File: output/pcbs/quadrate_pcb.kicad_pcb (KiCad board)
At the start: 2 copper layers, 99.2 x 99.2 mm, 19 parts

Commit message: ortho
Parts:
- added S18: , MX, F.Cu at (233.2, 195.2)
- moved S16 31.5 mm to (195.2, 195.2), turned to 0 degrees
- moved S17 24.5 mm to (214.2, 195.2), turned to 0 degrees
- moved S7 13.3 mm to (190.4, 152.4)
- moved S8 13.3 mm to (190.4, 133.3)
- moved S9 13.3 mm to (190.4, 114.3)
- moved S10 11.4 mm to (209.4, 152.4)
- moved S11 11.4 mm to (209.4, 133.3)
- moved S12 11.4 mm to (209.4, 114.3)
- moved S4 9.53 mm to (171.4, 152.4)
- moved S5 9.52 mm to (171.4, 133.3)
- moved S6 9.52 mm to (171.4, 114.3)
- moved S13 7.62 mm to (228.4, 152.4)
- moved TRRS1 7.62 mm to (241.7, 169.5)
- moved S14 7.62 mm to (228.4, 133.3)
- moved S15 7.62 mm to (228.4, 114.3)
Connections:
- net thumbfan_far_home renamed thumbfan_home_home
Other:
- board size 99.2 x 99.2 mm -> 100 x 100 mm

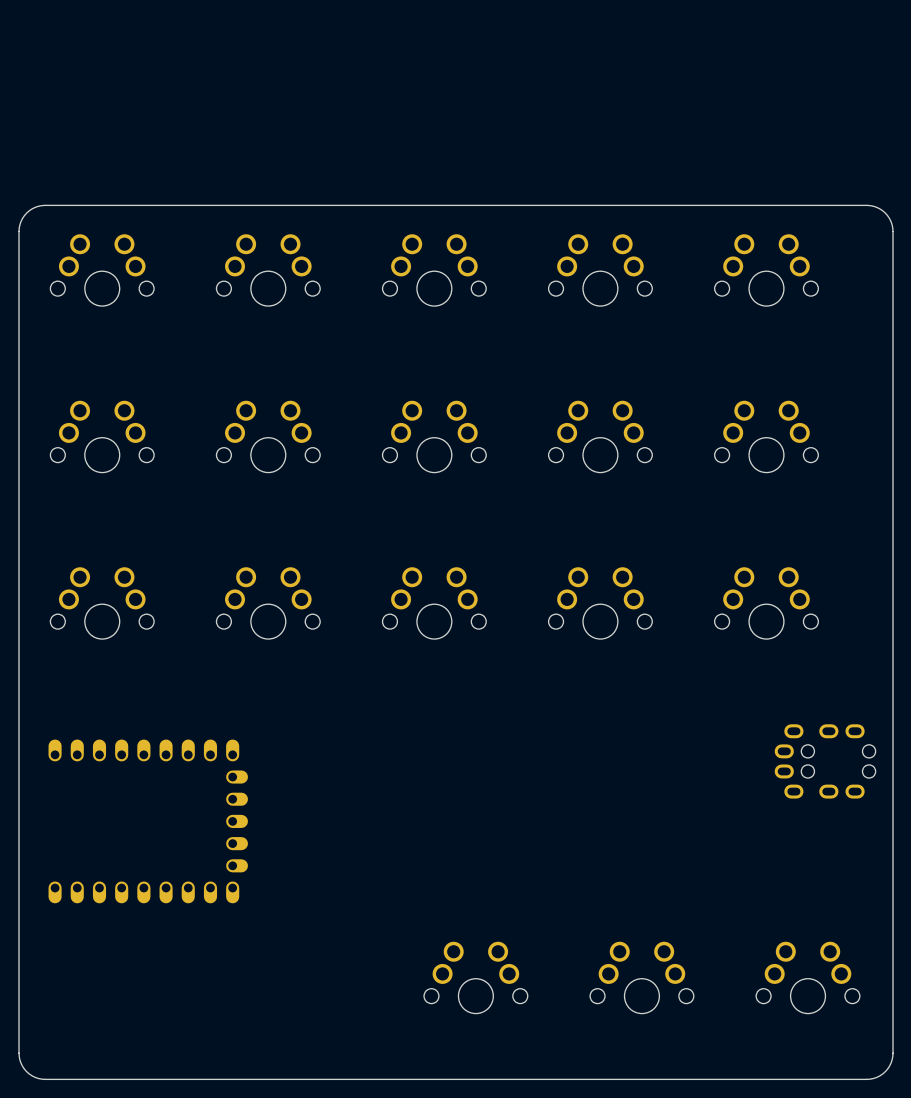
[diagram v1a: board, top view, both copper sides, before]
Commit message: rj45, columnar stagger
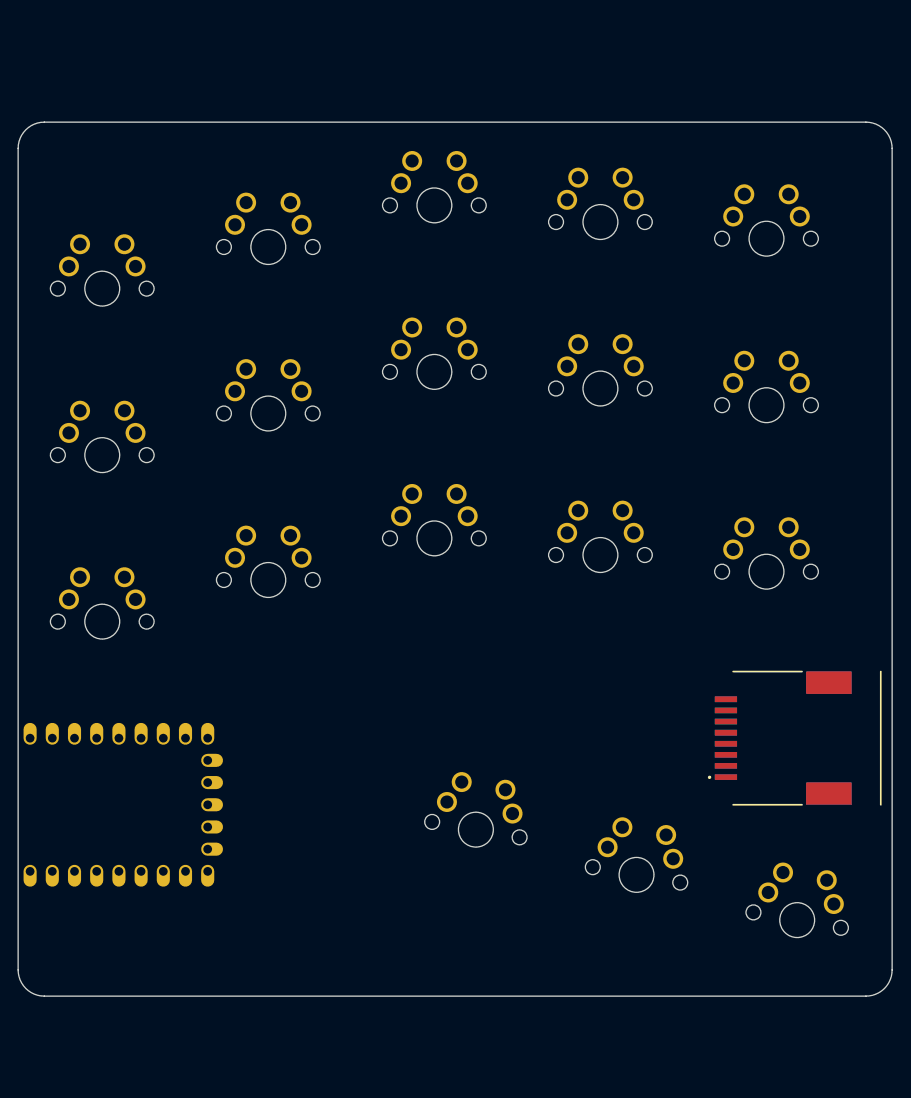
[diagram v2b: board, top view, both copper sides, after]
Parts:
- removed TRRS1: TRRS-PJ-320A-dual, TRRS-PJ-320A-dual
- added ?: , 44144-0003, F.Cu at (224.6, 165.7)
- moved S16 19.1 mm to (195.2, 176.2), turned to -10 degrees
- moved S17 13.9 mm to (213.5, 181.4), turned to -10 degrees
- moved S7 9.53 mm to (190.4, 142.9)
- moved S8 9.52 mm to (190.4, 123.8)
- moved S9 9.52 mm to (190.4, 104.8)
- moved S18 8.79 mm to (231.9, 186.6), turned to -10 degrees
- moved S10 7.62 mm to (209.4, 144.8)
- moved S11 7.62 mm to (209.4, 125.7)
- moved S12 7.62 mm to (209.4, 106.7)
- moved S13 5.72 mm to (228.4, 146.7)
- moved S14 5.71 mm to (228.4, 127.6)
- moved S15 5.71 mm to (228.4, 108.6)
- moved S4 4.76 mm to (171.4, 147.6)
- moved S5 4.76 mm to (171.4, 128.6)
- moved S6 4.76 mm to (171.4, 109.5)
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
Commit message: thumbfan placement splayed and a little more comfortable
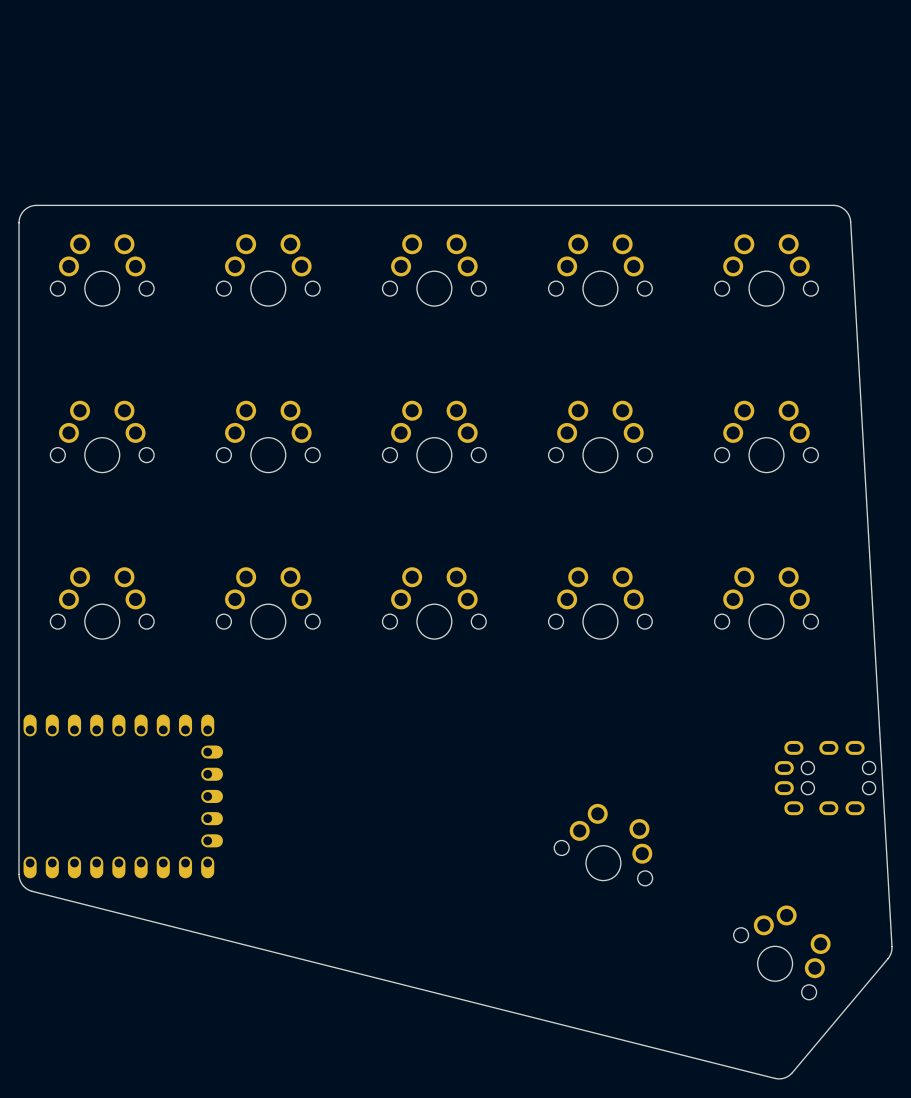
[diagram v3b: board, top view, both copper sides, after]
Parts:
- removed the ? at (224.6, 165.7)
- removed S18: , MX
- added TRRS1: TRRS-PJ-320A-dual, TRRS-PJ-320A-dual, F.Cu at (241.7, 171.5)
- moved S17 18.8 mm to (229.4, 191.5), turned to -40 degrees
- moved S16 15.1 mm to (209.7, 180.0), turned to -20 degrees
- moved S7 9.53 mm to (190.4, 152.4)
- moved S8 9.52 mm to (190.4, 133.3)
- moved S9 9.52 mm to (190.4, 114.3)
- moved S10 7.62 mm to (209.4, 152.4)
- moved S11 7.62 mm to (209.4, 133.3)
- moved S12 7.62 mm to (209.4, 114.3)
- moved S13 5.72 mm to (228.4, 152.4)
- moved S14 5.71 mm to (228.4, 133.3)
- moved S15 5.71 mm to (228.4, 114.3)
- moved S4 4.76 mm to (171.4, 152.4)
- moved S5 4.76 mm to (171.4, 133.3)
- moved S6 4.76 mm to (171.4, 114.3)
- moved ? 0.95 mm to (154.3, 172.4)
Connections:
- S17 pad 1: thumbfan_home_home -> thumbfan_far_home
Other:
- board size 100 x 100 mm -> 99.9 x 99.9 mm

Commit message: trying a janus knockoff...again
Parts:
- removed TRRS1: TRRS-PJ-320A-dual, TRRS-PJ-320A-dual
- added ?: , 44144-0003, F.Cu at (232.2, 101.0)
- added S18: , MX, F.Cu at (233.2, 173.8)
- moved ? 95.8 mm to (209.4, 94.1)
- moved S17 23.4 mm to (214.2, 173.8), turned to 0 degrees
- moved S16 15.9 mm to (195.2, 173.8), turned to 0 degrees
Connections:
- net thumbfan_far_home renamed thumbfan_home_home
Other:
- board size 99.9 x 99.9 mm -> 99.8 x 100 mm

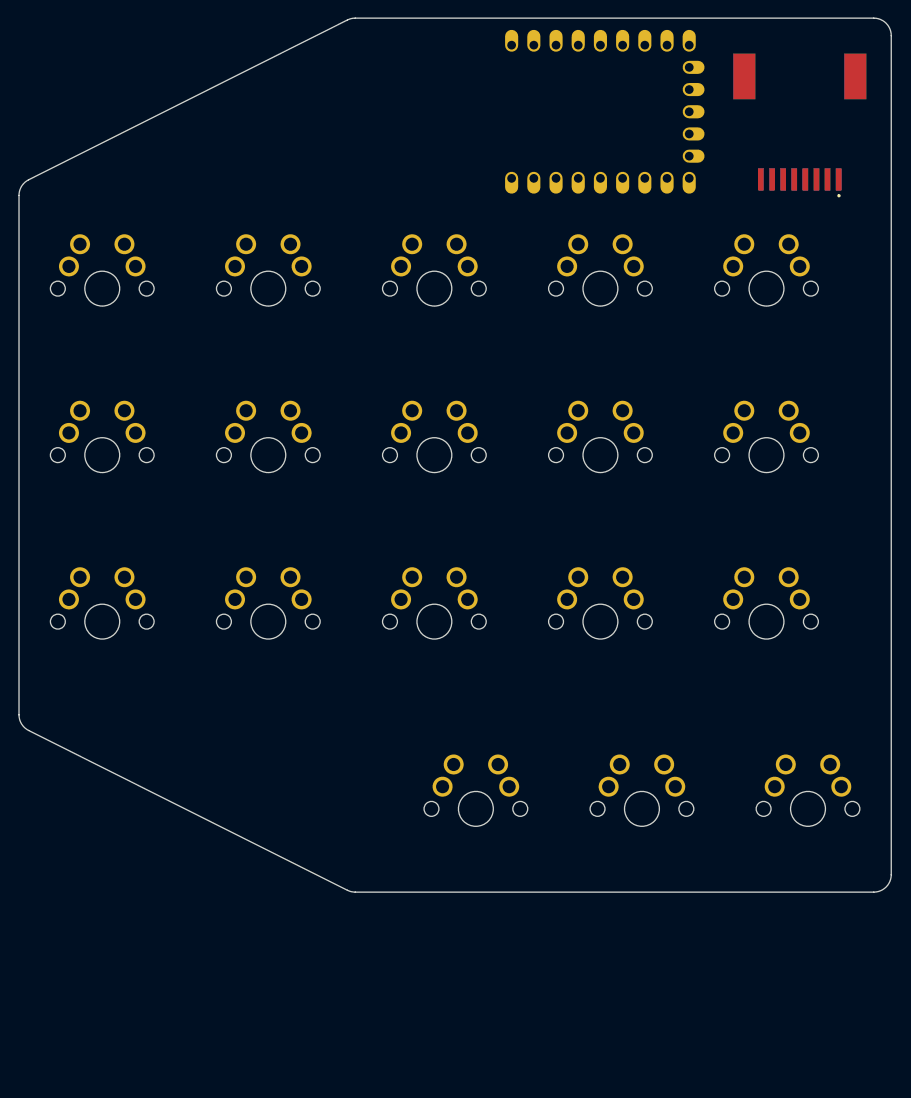
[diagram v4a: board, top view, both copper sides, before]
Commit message: mounting holes, holes for stacking PCBs
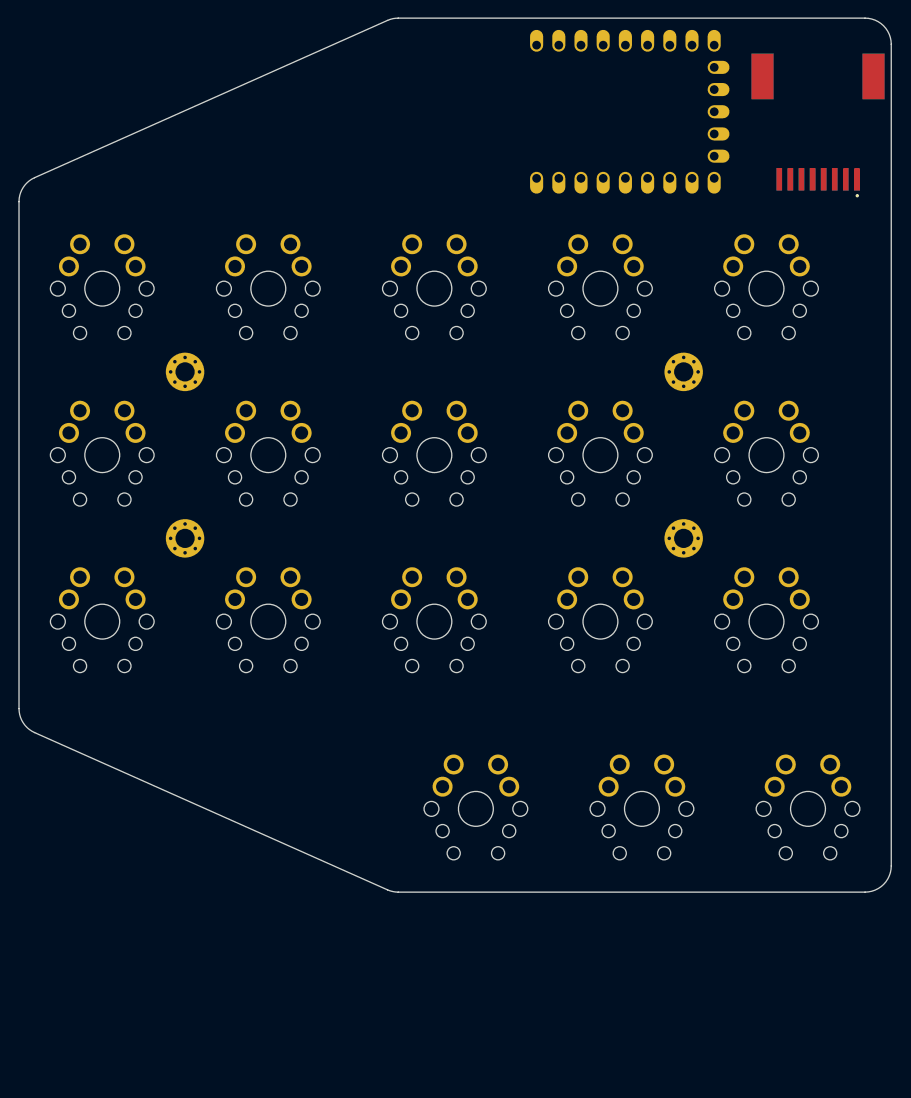
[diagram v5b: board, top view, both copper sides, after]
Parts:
- added _3: , MountingHole_2.2mm_M2_Pad_Via, F.Cu at (161.9, 123.8)
- added _4: , MountingHole_2.2mm_M2_Pad_Via, F.Cu at (161.9, 142.9)
- added _5: , MountingHole_2.2mm_M2_Pad_Via, F.Cu at (218.9, 123.8)
- added _6: , MountingHole_2.2mm_M2_Pad_Via, F.Cu at (218.9, 142.9)
- moved ? 2.86 mm to (212.3, 94.1)
- moved ? 2.10 mm to (234.3, 101.0)
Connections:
- ? pad 1: GP0 -> matrix_pinky_top
- ? pad 11: GP10 -> matrix_middle_bottom
- ? pad 12: GP11 -> matrix_inner_bottom
- ? pad 13: GP12 -> matrix_inner_home
- ? pad 14: GP13 -> matrix_inner_top
- ? pad 15: GP14 -> thumbfan_far_home
- ? pad 16: GP15 -> thumbfan_home_home
- ? pad 17: GP26 -> thumbfan_near_home
- ? pad 18: GP27 -> matrix_index_top
- ? pad 19: GP28 -> matrix_index_home
- ? pad 2: GP1 -> matrix_pinky_home
- ? pad 20: GP29 -> matrix_index_bottom
- ? pad 3: GP2 -> matrix_pinky_bottom
- ? pad 4: GP3 -> matrix_ring_top
- ? pad 5: GP4 -> matrix_ring_home
- ? pad 6: GP5 -> matrix_ring_bottom
- ? pad 7: GP6 -> matrix_middle_top
- ? pad 8: GP7 -> matrix_middle_home
- ? pad 3: GP0 -> GP8
- ? pad 4: GP0 -> GP8
- ? pad 5: GP1 -> GP9
- ? pad 6: GP1 -> GP9
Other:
- outline, holes or cut-outs redrawn
